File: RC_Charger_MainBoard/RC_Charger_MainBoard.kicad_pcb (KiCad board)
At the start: 2 copper layers, 200 x 100 mm, 91 parts, among them J1 Conn_02x03_Odd_Even, J3 SPK1, J4 SPK2, J9 Conn_02x03_Odd_Even, U1 NUCLEO-H745ZI-Q, U13 TAS5825MRHB, U3 L7805, U4 LM5001MA, U5 TPS54560BDDA, U6 TPS54560BDDA

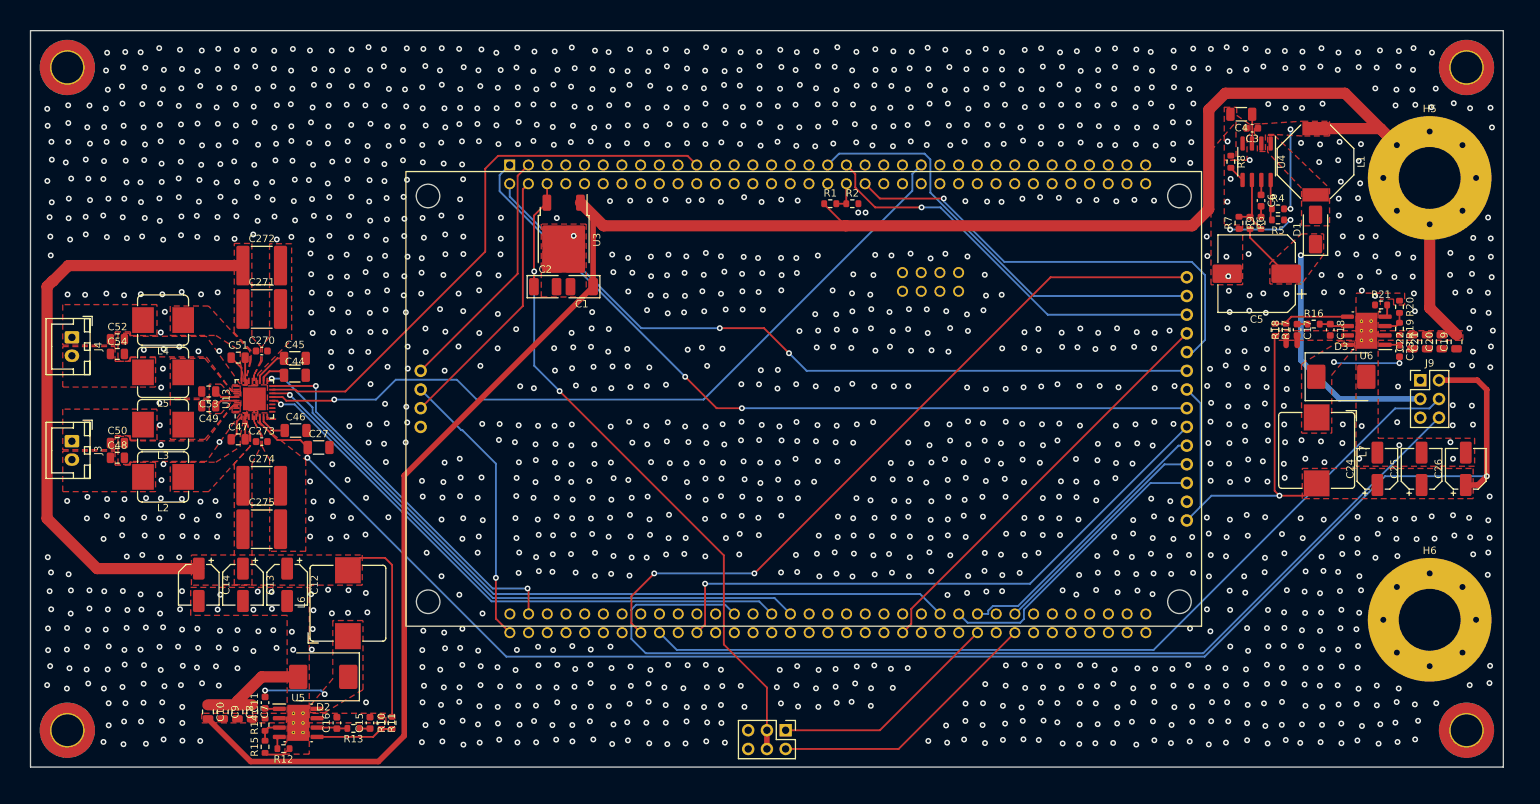
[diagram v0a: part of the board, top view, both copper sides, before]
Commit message: Change MainBoard Serov Position
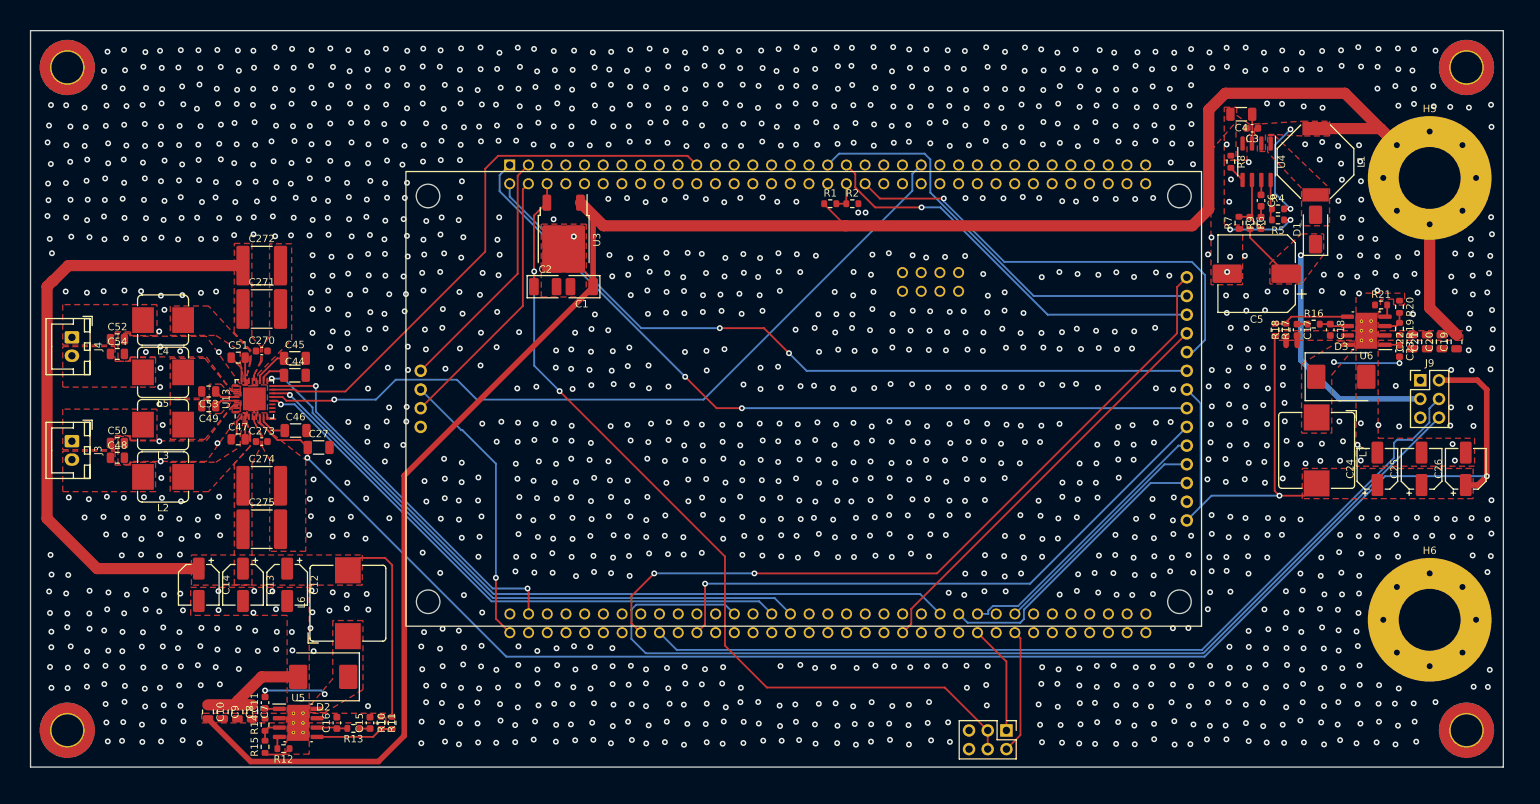
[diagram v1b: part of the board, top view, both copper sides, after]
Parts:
- moved J1 30.0 mm to (182.5, 145.0)
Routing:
- net +5V: track 92.7 -> 119.3 mm
- net SERVO2: track 37.7 -> 16.9 mm
- net SERVO1: track 31.5 -> 14.9 mm
- net T_IRQ: track 98.8 -> 102.5 mm
- net IO_SDA: track 120.9 -> 123.2 mm
- net VIN: track 307.9 -> 309.7 mm
- net GND: vias 1691 -> 1712

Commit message: Change components for costdown
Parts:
- removed C15: 4.7u, Capacitor_SMD:C_0603_1608Metric
- removed C16: 47p, Capacitor_SMD:C_0603_1608Metric
- removed C17: 12n, Capacitor_SMD:C_0603_1608Metric
- removed C18: 10p, Capacitor_SMD:C_0603_1608Metric
- removed C19, C20, C21, C22: 2.2u, Capacitor_SMD:C_0805_2012Metric
- removed C24, C25: 47u, Capacitor_SMD:CP_Elec_5x5.8
- removed C271, C272, C274, C275: 22u, Capacitor_SMD:C_2220_5650Metric
- removed R12, R21: 243k, Resistor_SMD:R_0603_1608Metric
- removed R13: 16.9k, Resistor_SMD:R_0603_1608Metric
- removed R14, R19: 442k, Resistor_SMD:R_0603_1608Metric
- removed R15, R20: 90.9k, Resistor_SMD:R_0603_1608Metric
- removed R16: 12.1k, Resistor_SMD:R_0603_1608Metric
- added C28: 22u, Capacitor_SMD:CP_Elec_6.3x5.4, F.Cu at (81.4, 81.9)
- added C29: 22u, Capacitor_SMD:CP_Elec_6.3x5.4, F.Cu at (81.4, 89.1)
- added C30: 22u, Capacitor_SMD:CP_Elec_6.3x5.4, F.Cu at (82.4, 110.3)
- added C31: 22u, Capacitor_SMD:CP_Elec_6.3x5.4, F.Cu at (82.4, 117.5)
- C10, C7, C8, C9: value 2.2u -> 68u; footprint Capacitor_SMD:C_0805_2012Metric -> Capacitor_SMD:CP_Elec_6.3x7.7
- C11, C23, C3: value 100n -> 0.1u
- C12, C13: value 47u -> 0.1u; footprint Capacitor_SMD:CP_Elec_5x5.8 -> Capacitor_SMD:C_0603_1608Metric
- C14, C26: value 47u -> 560u; footprint Capacitor_SMD:CP_Elec_5x5.8 -> Capacitor_SMD:CP_Elec_10x10
- C27, C44, C45, C46: value 1uf -> 1u
- C5: footprint Capacitor_SMD:CP_Elec_10x10 -> Capacitor_SMD:CP_Elec_4x5.7
- D2, D3: value B560C -> SS54F; footprint Diode_SMD:D_SMC -> Diode_SMD:D_SMA
- L1: footprint Inductor_SMD:L_Bourns-SRU1028_10.0x10.0mm -> Inductor_SMD:L_Taiyo-Yuden_NR-80xx_HandSoldering
- L2, L3, L4, L5: footprint Inductor_SMD:L_Bourns_SRP7028A_7.3x6.6mm -> Inductor_SMD:L_Taiyo-Yuden_NR-50xx_HandSoldering
- L6, L7: value 7.2u -> 15u; footprint Inductor_SMD:L_Bourns_SRP1038C_10.0x10.0mm -> Inductor_SMD:L_Bourns_SRR1260
- R10: value 53.6k -> 10k
- R11: value 10.2k -> 3.24k
- R17: value 36.5k -> 10k
- R18: value 11.7k -> 5.9k
- U5, U6: value TPS54560BDDA -> TPS5430DDA
- moved U6 157.6 mm to (81.9, 140.5)
- moved D3 155.3 mm to (80.3, 145.0)
- moved C9 154.4 mm to (223.6, 96.8), turned to 0 degrees
- moved C7 152.9 mm to (223.6, 89.6), turned to 0 degrees
- moved U5 142.5 mm to (223.6, 105.5), turned to 90 degrees
- moved C12 140.8 mm to (223.6, 101.1), turned to 0 degrees
- moved D2 133.6 mm to (219.1, 104.0), turned to -90 degrees
- moved C23 23.8 mm to (217.3, 108.4), turned to 180 degrees
- moved R17 19.0 mm to (227.2, 107.7)
- moved R11 17.9 mm to (81.2, 136.8), turned to 0 degrees
- moved R10 16.6 mm to (84.2, 136.8), turned to 0 degrees
- moved C14 15.7 mm to (88.2, 128.2), turned to 180 degrees
- moved R18 15.6 mm to (227.2, 104.7), turned to -90 degrees
- moved C13 15.3 mm to (77.5, 140.5), turned to 90 degrees
- moved L6 12.5 mm to (92.2, 140.2)
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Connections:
- C10 pad 1: GND -> VIN
- C10 pad 2: VIN -> GND
- C11 pad 1: Net-(U5-BOOT) -> Net-(U6-BOOT)
- C11 pad 2: Net-(D2-K) -> Net-(D3-K)
- C12 pad 1: /5V Buck/VOUT -> VIN
- C13 pad 1: /5V Buck/VOUT -> VIN
- C23 pad 1: Net-(U6-BOOT) -> Net-(U5-BOOT)
- C23 pad 2: Net-(D3-K) -> Net-(D2-K)
- C7 pad 1: GND -> VIN
- C7 pad 2: VIN -> GND
- C8 pad 1: GND -> VIN
- C8 pad 2: VIN -> GND
- C9 pad 1: GND -> VIN
- C9 pad 2: VIN -> GND
- J9 pad 1: +24V -> unconnected-(J9-Pin_1-Pad1)
- L6 pad 1: Net-(D2-K) -> Net-(D3-K)
- L7 pad 1: Net-(D3-K) -> Net-(D2-K)
- U5 pad 2: VIN -> unconnected-(U5-NC-Pad2)
- U5 pad 3: Net-(U5-EN) -> unconnected-(U5-NC-Pad3)
- U5 pad 4: Net-(U5-RT/CLK) -> /3V3 Buck/FB
- U5 pad 5: /5V Buck/FB -> VIN
- U5 pad 6: /5V Buck/COMP -> GND
- U5 pad 7: GND -> VIN
- U6 pad 2: VIN -> unconnected-(U6-NC-Pad2)
- U6 pad 3: Net-(U6-EN) -> unconnected-(U6-NC-Pad3)
- U6 pad 4: Net-(U6-RT/CLK) -> /5V Buck/FB
- U6 pad 5: /3V3 Buck/FB -> VIN
- U6 pad 6: /3V3 Buck/COMP -> GND
- U6 pad 7: GND -> VIN
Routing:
- net GND: track 33.4 -> 10.8 mm, vias 1712 -> 4
- net VIN: track 309.7 -> 329.2 mm, vias 2 -> 6
- net S_PWR: track 269.7 -> 283.2 mm
- net Net-(D3-K): track 9.84 -> 0.00 mm, vias 2 -> 0
- net Net-(D2-K): track 9.18 -> 0.00 mm, vias 2 -> 0
- net /5V Buck/FB: track 10.6 -> 3.63 mm
- net Net-(U5-BOOT): track 1.97 -> 7.28 mm
- net /5V Buck/COMP: track 4.18 -> 0.00 mm
- net /3V3 Buck/COMP: track 3.87 -> 0.00 mm
- net Net-(U5-EN): track 3.47 -> 0.00 mm
- net Net-(U6-EN): track 3.47 -> 0.00 mm
- net /3V3 Buck/FB: track 10.6 -> 7.26 mm
- net VCC: track 40.8 -> 38.4 mm
- net Net-(U5-RT/CLK): track 1.70 -> 0.00 mm
- net Net-(U6-RT/CLK): track 1.70 -> 0.00 mm
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
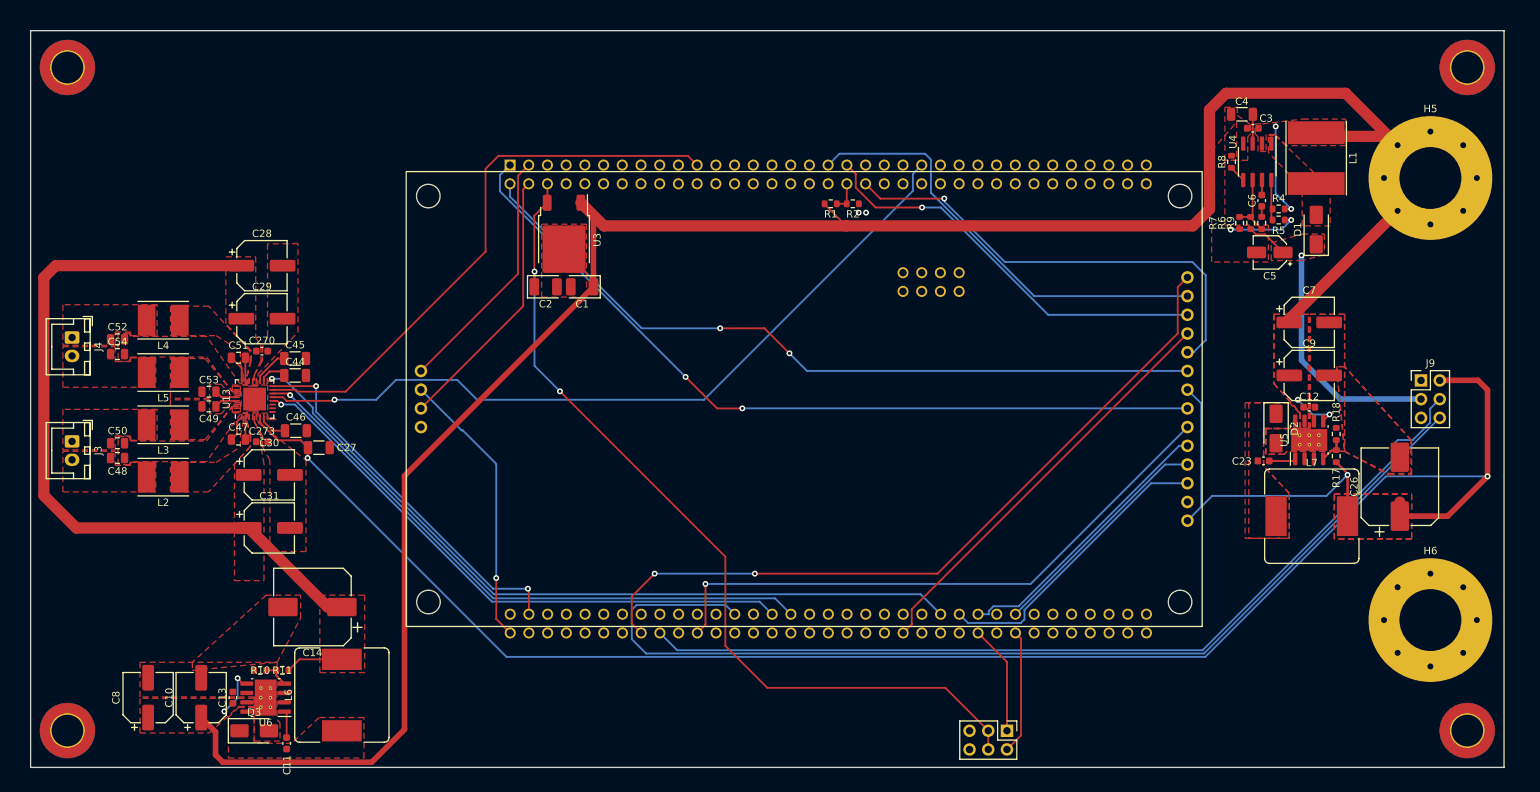
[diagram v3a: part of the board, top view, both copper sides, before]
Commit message: Add full bom and final pcb design
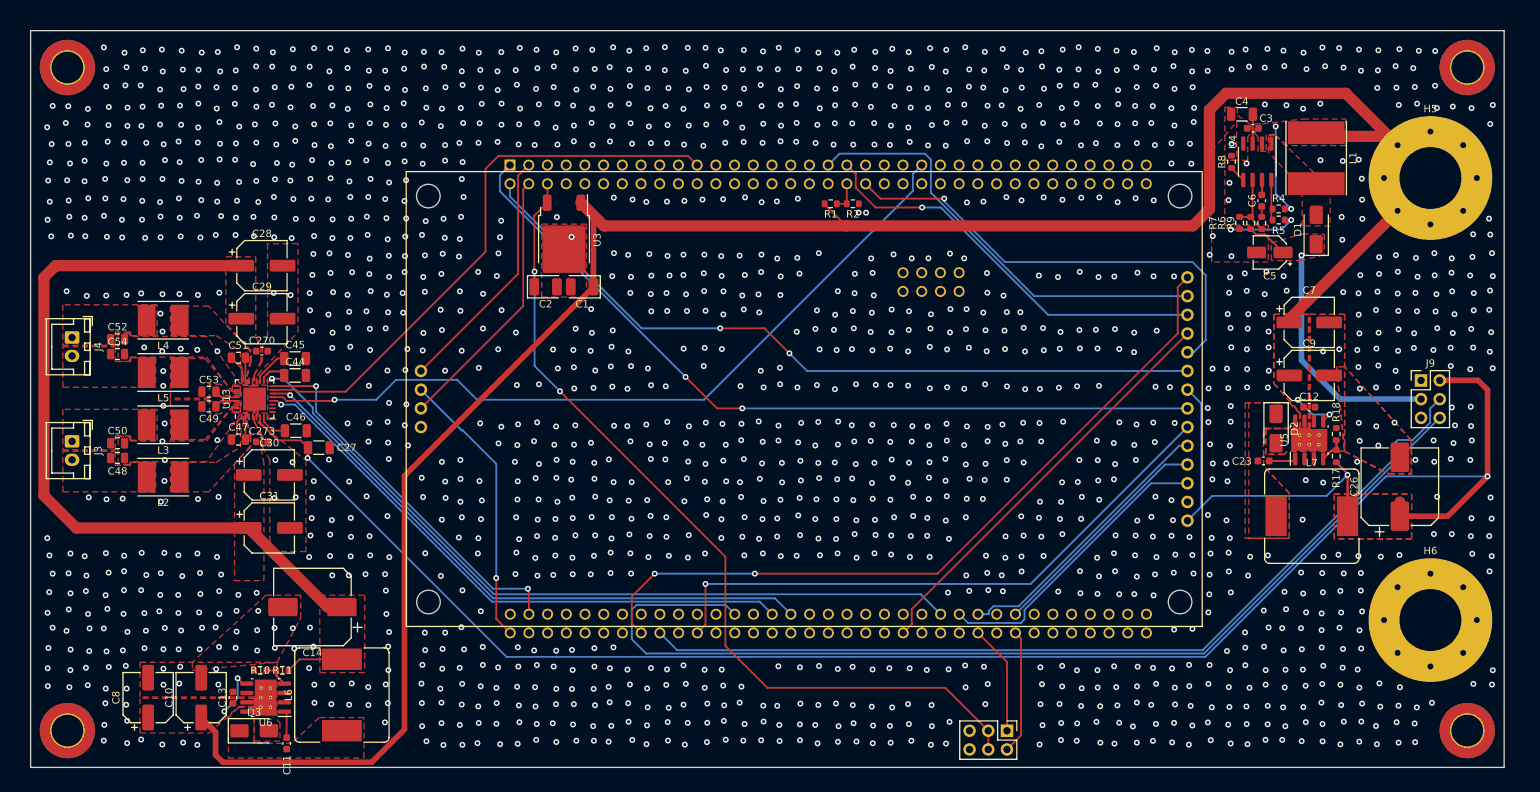
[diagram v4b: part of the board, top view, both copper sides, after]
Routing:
- net GND: vias 4 -> 1707
